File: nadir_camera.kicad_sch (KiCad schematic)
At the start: 54 parts, among them J1 MOLEX_5051102491, J12 Conn 02x05 1.27mm, J13 Micro_SD_Card, J14 USB_C_Receptacle_USB2.0, SW5 KMR2x, SW6 CAS-120TA, U24 STM32H743VITx, U25 USBLC6-2SC6, Y4 12MHz/7pF

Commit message: Initial placement for 2nd MCU
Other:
- note added: "Datasheet: https://www.st.com/resource/en/datasheet/stm32h743vi.pdf (See pg. 209 for power supply instructions)"
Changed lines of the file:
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@@
 	(text "MCU (STM32H743VITx)"
 		(exclude_from_sim no)
-		(at 45.72 25.4 0)
+		(at 56.388 23.876 0)
 		(effects
 			(font
@@
 		)
 	)
+	(text "Datasheet: https://www.st.com/resource/en/datasheet/stm32h743vi.pdf\n(See pg. 209 for power supply instructions)"
+		(exclude_from_sim no)
+		(at 19.558 27.686 0)
+		(effects
+			(font
+				(size 1.27 1.27)
+			)
+			(justify left)
+		)
+	)

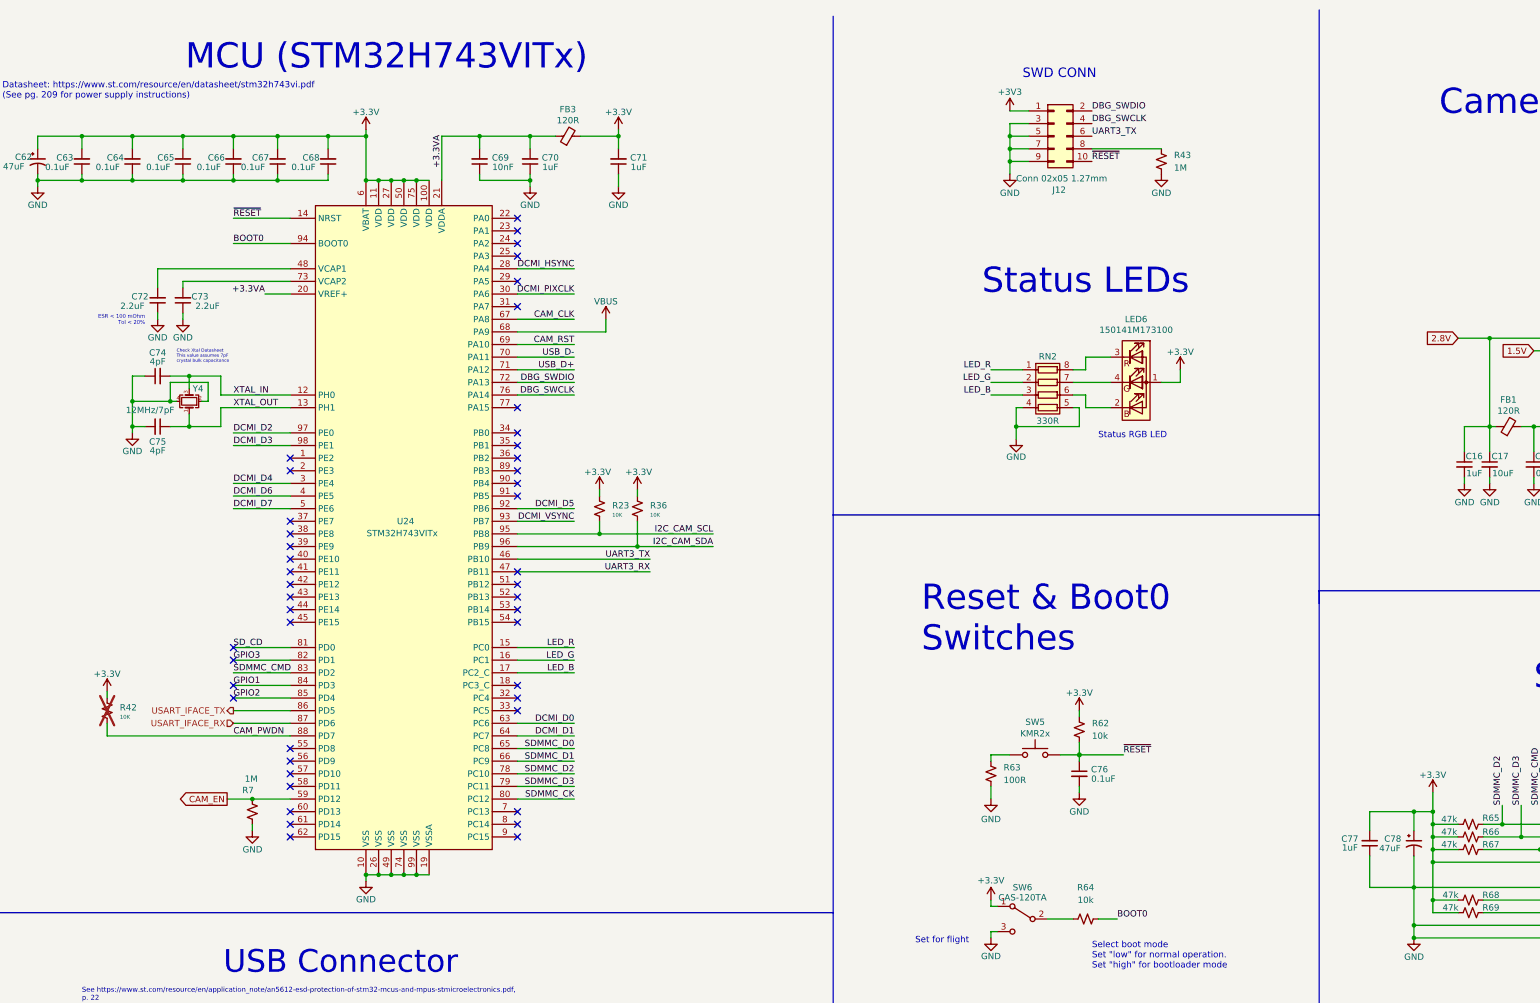
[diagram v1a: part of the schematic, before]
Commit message: Minor fixes
Closes #12
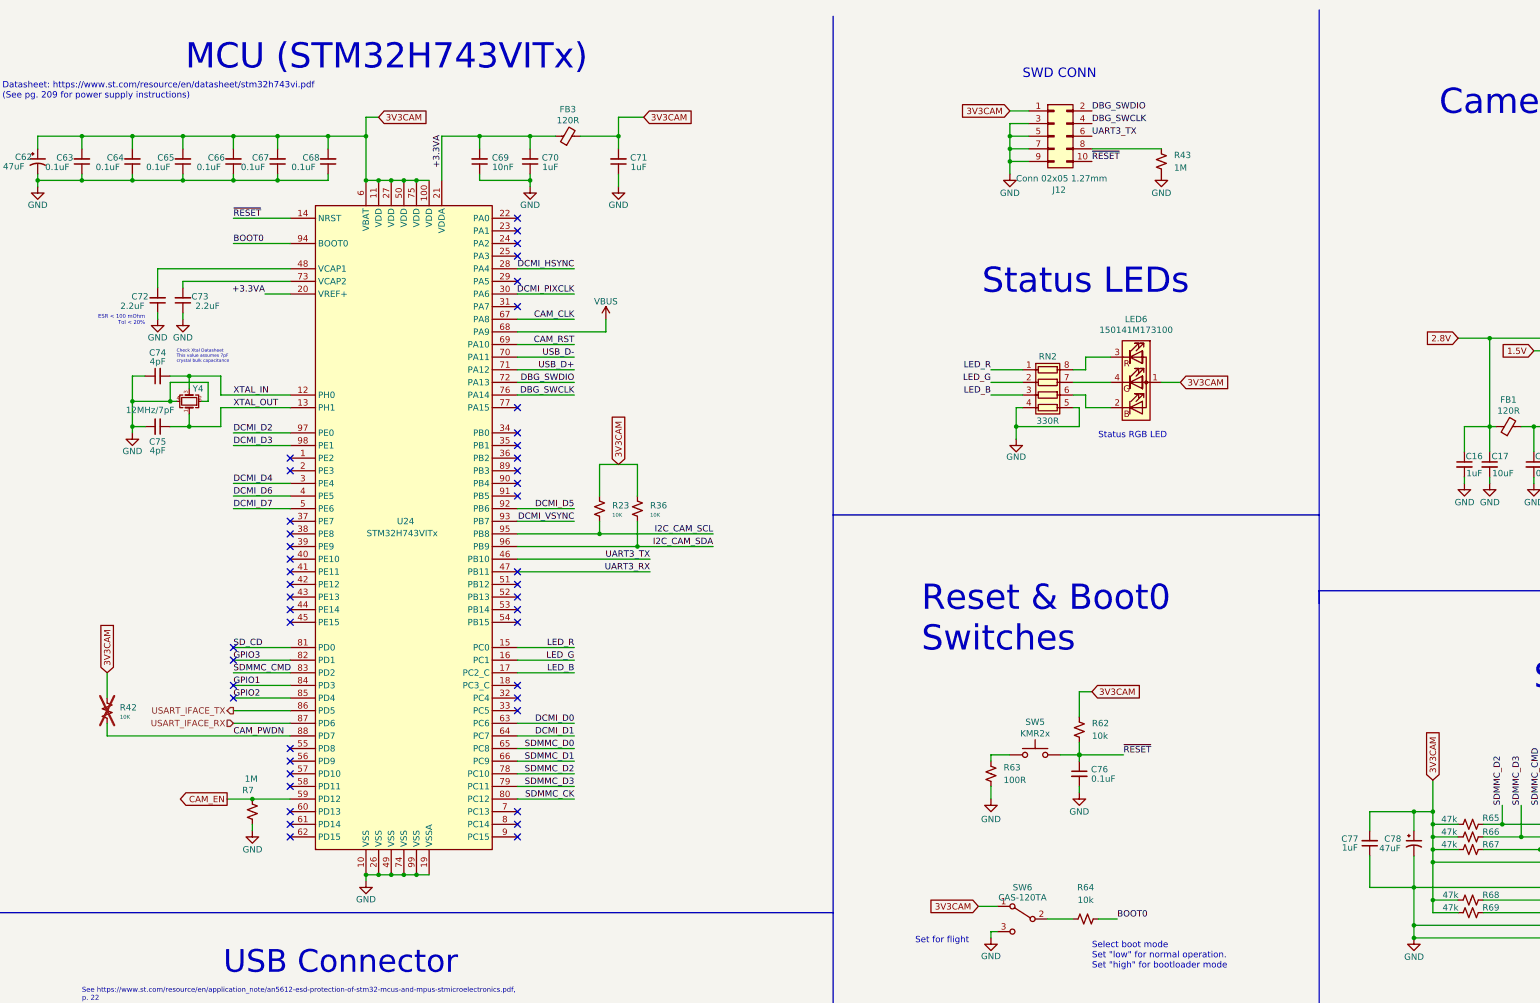
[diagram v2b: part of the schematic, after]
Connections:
- net +3V3 is gone; now on net 3V3CAM: J12.1 (Pin_1)
- net +3.3V renamed 3V3CAM
